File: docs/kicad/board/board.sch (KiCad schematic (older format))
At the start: 17 parts, among them J1 VIN, J10 WHEEL_4, J11 FLAG, J12 LED, J13 COMPASS, J14 SWITCH, J2 LEFT, J3 RIGHT, J4 UNUSED, J5 ARM, J6 LID, J7 WHEEL_1, J8 WHEEL_2, J9 WHEEL_3, SW1 BUTTON_1, SW2 BUTTON_2, U1 ARDUINO_NANO

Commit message: Built version 2 for Daniel
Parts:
- removed J4: UNUSED, cnc3018-PCB:my4pin, symbol Connector_Generic:Conn_01x04
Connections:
- net U_IR: no longer names the net of U1.12 (A0)
- net U_SENS: no longer names the net of U1.15 (D13)
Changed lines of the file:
@@
 Text GLabel 4850 3050 1    50   Input ~ 0
 R_IR
-Text GLabel 5150 3050 1    50   Input ~ 0
-U_IR
 Text GLabel 4550 3050 1    50   Input ~ 0
 L_SENS
 Text GLabel 4950 3050 1    50   Input ~ 0
 R_SENS
-Text GLabel 5450 3050 1    50   Input ~ 0
-U_SENS
 Text GLabel 4650 3850 3    50   Input ~ 0
 WHEEL_1
@@
 	-1   0    0    1
 $EndComp
-$Comp
-L Connector_Generic:Conn_01x04 J4
-U 1 1 63300773
-P 4650 1350
-F 0 "J4" V 4850 1350 50  0000 R CNN
-F 1 "UNUSED" V 4750 1300 50  0000 C CNN
-F 2 "cnc3018-PCB:my4pin" H 4650 1350 50  0001 C CNN
-F 3 "~" H 4650 1350 50  0001 C CNN
-	1    4650 1350
-	0    -1   -1   0
-$EndComp
-$Comp
-L power:GND #PWR06
-U 1 1 63300779
-P 4550 1550
-F 0 "#PWR06" H 4550 1300 50  0001 C CNN
-F 1 "GND" V 4550 1350 50  0000 C CNN
-F 2 "" H 4550 1550 50  0001 C CNN
-F 3 "" H 4550 1550 50  0001 C CNN
-	1    4550 1550
-	1    0    0    -1
-$EndComp
-$Comp
-L power:+5V #PWR07
-U 1 1 6330077F
-P 4650 1550
-F 0 "#PWR07" H 4650 1400 50  0001 C CNN
-F 1 "+5V" V 4650 1750 50  0000 C CNN
-F 2 "" H 4650 1550 50  0001 C CNN
-F 3 "" H 4650 1550 50  0001 C CNN
-	1    4650 1550
-	-1   0    0    1
-$EndComp
 Text GLabel 3700 1550 3    50   Input ~ 0
 L_SENS
-Text GLabel 4850 1550 3    50   Input ~ 0
-U_SENS
 Text GLabel 4300 1550 3    50   Input ~ 0
 R_SENS
 Text GLabel 3600 1550 3    50   Input ~ 0
 L_IR
-Text GLabel 4750 1550 3    50   Input ~ 0
-U_IR
 Text GLabel 4200 1550 3    50   Input ~ 0
 R_IR

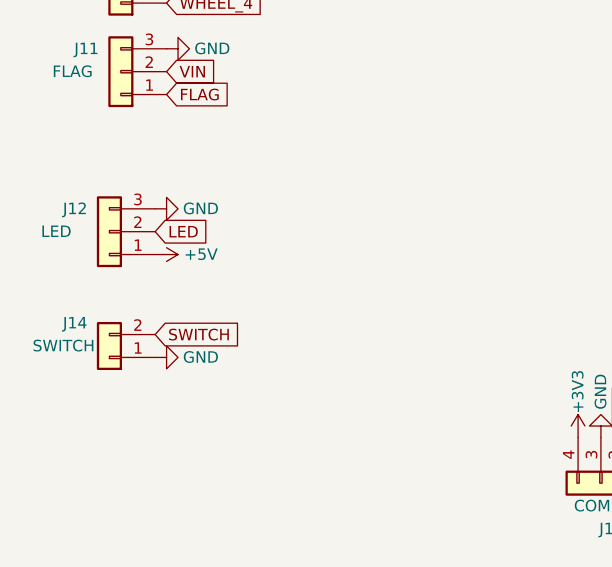
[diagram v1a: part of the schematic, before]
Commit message: created 3D rendering of PCB with my new kicad footprint files
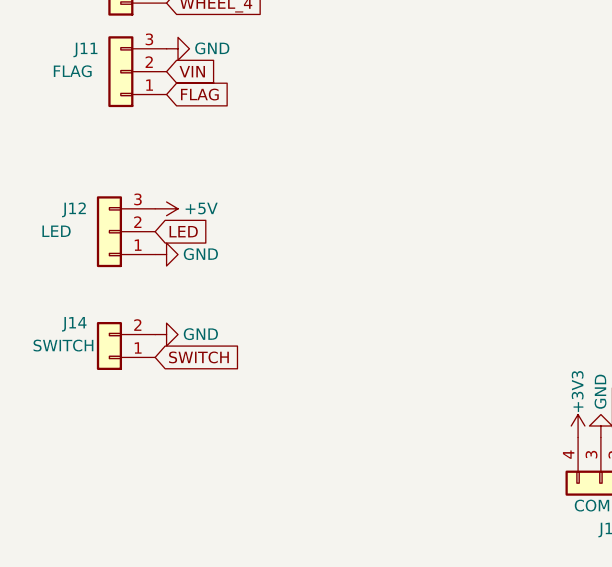
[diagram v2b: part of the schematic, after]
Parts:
- J1, J14: footprint cnc3018-PCB:my2pin -> 0_my_footprints:myJSTx02
- J10, J11, J5, J6, J7, J8, J9: footprint cnc3018-PCB:my3pin -> Connector_PinHeader_2.54mm:PinHeader_1x03_P2.54mm_Vertical
- J12: footprint cnc3018-PCB:my3pin -> 0_my_footprints:myJSTx03
- J13: footprint cnc3018-PCB:my4pin -> 0_my_footprints:myPinSocket_1x04
- J2, J3: footprint cnc3018-PCB:my4pin -> 0_my_footprints:myJSTx04
- SW1, SW2: footprint cnc3018-PCB:right_angle_button -> 0_my_footprints:myButtonAngled
- U1: footprint cnc3018-PCB:ARDUINO_NANO -> 0_my_footprints:myArduinoNano
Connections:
- net +5V: now also J12.3 (Pin_3); no longer J12.1 (Pin_1)
- net GND: now also J12.1 (Pin_1), J14.2 (Pin_2); no longer J12.3 (Pin_3), J14.1 (Pin_1)
- net SWITCH: now also J14.1 (Pin_1); no longer J14.2 (Pin_2)
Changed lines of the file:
@@
 F 0 "U1" H 5528 3496 50  0000 L CNN
 F 1 "ARDUINO_NANO" H 5528 3405 50  0000 L CNN
-F 2 "cnc3018-PCB:ARDUINO_NANO" H 4350 3450 50  0001 C CNN
+F 2 "0_my_footprints:myArduinoNano" H 4350 3450 50  0001 C CNN
 F 3 "" H 4350 3450 50  0001 C CNN
 	1    4700 3450
@@
 F 0 "J1" H 1550 900 50  0000 C CNN
 F 1 "VIN" H 1550 1000 50  0000 C CNN
-F 2 "cnc3018-PCB:my2pin" H 1400 1050 50  0001 C CNN
+F 2 "0_my_footprints:myJSTx02" H 1400 1050 50  0001 C CNN
 F 3 "~" H 1400 1050 50  0001 C CNN
 	1    1400 1050
@@
 F 0 "J5" H 1550 1600 50  0000 C CNN
 F 1 "ARM" H 1650 1700 50  0000 R CNN
-F 2 "cnc3018-PCB:my3pin" H 1400 1700 50  0001 C CNN
+F 2 "Connector_PinHeader_2.54mm:PinHeader_1x03_P2.54mm_Vertical" H 1400 1700 50  0001 C CNN
 F 3 "~" H 1400 1700 50  0001 C CNN
 	1    1400 1700
@@
 F 0 "J6" H 1550 2000 50  0000 C CNN
 F 1 "LID" H 1650 2100 50  0000 R CNN
-F 2 "cnc3018-PCB:my3pin" H 1400 2100 50  0001 C CNN
+F 2 "Connector_PinHeader_2.54mm:PinHeader_1x03_P2.54mm_Vertical" H 1400 2100 50  0001 C CNN
 F 3 "~" H 1400 2100 50  0001 C CNN
 	1    1400 2100
@@
 F 0 "J7" H 1550 2400 50  0000 C CNN
 F 1 "WHEEL_1" H 1850 2500 50  0000 R CNN
-F 2 "cnc3018-PCB:my3pin" H 1400 2500 50  0001 C CNN
+F 2 "Connector_PinHeader_2.54mm:PinHeader_1x03_P2.54mm_Vertical" H 1400 2500 50  0001 C CNN
 F 3 "~" H 1400 2500 50  0001 C CNN
 	1    1400 2500
@@
 F 0 "J8" H 1550 2800 50  0000 C CNN
 F 1 "WHEEL_2" H 1850 2900 50  0000 R CNN
-F 2 "cnc3018-PCB:my3pin" H 1400 2900 50  0001 C CNN
+F 2 "Connector_PinHeader_2.54mm:PinHeader_1x03_P2.54mm_Vertical" H 1400 2900 50  0001 C CNN
 F 3 "~" H 1400 2900 50  0001 C CNN
 	1    1400 2900
@@
 F 0 "J9" H 1550 3200 50  0000 C CNN
 F 1 "WHEEL_3" H 1850 3300 50  0000 R CNN
-F 2 "cnc3018-PCB:my3pin" H 1400 3300 50  0001 C CNN
+F 2 "Connector_PinHeader_2.54mm:PinHeader_1x03_P2.54mm_Vertical" H 1400 3300 50  0001 C CNN
 F 3 "~" H 1400 3300 50  0001 C CNN
 	1    1400 3300
@@
 F 0 "J10" H 1550 3600 50  0000 C CNN
 F 1 "WHEEL_4" H 1850 3700 50  0000 R CNN
-F 2 "cnc3018-PCB:my3pin" H 1400 3700 50  0001 C CNN
+F 2 "Connector_PinHeader_2.54mm:PinHeader_1x03_P2.54mm_Vertical" H 1400 3700 50  0001 C CNN
 F 3 "~" H 1400 3700 50  0001 C CNN
 	1    1400 3700
@@
 F 0 "J11" H 1550 4000 50  0000 C CNN
 F 1 "FLAG" H 1700 4100 50  0000 R CNN
-F 2 "cnc3018-PCB:my3pin" H 1400 4100 50  0001 C CNN
+F 2 "Connector_PinHeader_2.54mm:PinHeader_1x03_P2.54mm_Vertical" H 1400 4100 50  0001 C CNN
 F 3 "~" H 1400 4100 50  0001 C CNN
 	1    1400 4100
@@
 F 0 "J2" V 3700 1350 50  0000 R CNN
 F 1 "LEFT" V 3600 1300 50  0000 C CNN
-F 2 "cnc3018-PCB:my4pin" H 3500 1350 50  0001 C CNN
+F 2 "0_my_footprints:myJSTx04" H 3500 1350 50  0001 C CNN
 F 3 "~" H 3500 1350 50  0001 C CNN
 	1    3500 1350
@@
 F 0 "J3" V 4300 1350 50  0000 R CNN
 F 1 "RIGHT" V 4200 1300 50  0000 C CNN
-F 2 "cnc3018-PCB:my4pin" H 4100 1350 50  0001 C CNN
+F 2 "0_my_footprints:myJSTx04" H 4100 1350 50  0001 C CNN
 F 3 "~" H 4100 1350 50  0001 C CNN
 	1    4100 1350
@@
 F 0 "J12" H 1500 4700 50  0000 C CNN
 F 1 "LED" H 1650 4800 50  0000 R CNN
-F 2 "cnc3018-PCB:my3pin" H 1350 4800 50  0001 C CNN
+F 2 "0_my_footprints:myJSTx03" H 1350 4800 50  0001 C CNN
 F 3 "~" H 1350 4800 50  0001 C CNN
 	1    1350 4800
@@
 L power:GND #PWR022
 U 1 1 63327EFF
+P 1550 4900
+F 0 "#PWR022" H 1550 4650 50  0001 C CNN
+F 1 "GND" V 1550 4700 50  0000 C CNN
+F 2 "" H 1550 4900 50  0001 C CNN
+F 3 "" H 1550 4900 50  0001 C CNN
+	1    1550 4900
+	0    -1   -1   0
+$EndComp
+$Comp
+L power:+5V #PWR023
+U 1 1 6332BC14
 P 1550 4700
-F 0 "#PWR022" H 1550 4450 50  0001 C CNN
-F 1 "GND" V 1550 4500 50  0000 C CNN
+F 0 "#PWR023" H 1550 4550 50  0001 C CNN
+F 1 "+5V" V 1550 4900 50  0000 C CNN
 F 2 "" H 1550 4700 50  0001 C CNN
 F 3 "" H 1550 4700 50  0001 C CNN
 	1    1550 4700
-	0    -1   -1   0
-$EndComp
-$Comp
-L power:+5V #PWR023
-U 1 1 6332BC14
-P 1550 4900
-F 0 "#PWR023" H 1550 4750 50  0001 C CNN
-F 1 "+5V" V 1550 5100 50  0000 C CNN
-F 2 "" H 1550 4900 50  0001 C CNN
-F 3 "" H 1550 4900 50  0001 C CNN
-	1    1550 4900
 	0    1    1    0
 $EndComp
@@
 F 0 "J13" V 3800 5900 50  0000 R CNN
 F 1 "COMPASS" V 3700 5850 50  0000 C CNN
-F 2 "cnc3018-PCB:my4pin" H 3600 5900 50  0001 C CNN
+F 2 "0_my_footprints:myPinSocket_1x04" H 3600 5900 50  0001 C CNN
 F 3 "~" H 3600 5900 50  0001 C CNN
 	1    3600 5900
@@
 F 0 "SW1" H 6850 1935 50  0000 C CNN
 F 1 "BUTTON_1" H 6850 1844 50  0000 C CNN
-F 2 "cnc3018-PCB:right_angle_button" H 6850 1700 50  0001 C CNN
+F 2 "0_my_footprints:myButtonAngled" H 6850 1700 50  0001 C CNN
 F 3 "~" H 6850 1700 50  0001 C CNN
 	1    6850 1700
@@
 F 0 "SW2" H 6850 2385 50  0000 C CNN
 F 1 "BUTTON_2" H 6850 2294 50  0000 C CNN
-F 2 "cnc3018-PCB:right_angle_button" H 6850 2150 50  0001 C CNN
+F 2 "0_my_footprints:myButtonAngled" H 6850 2150 50  0001 C CNN
 F 3 "~" H 6850 2150 50  0001 C CNN
 	1    6850 2150
@@
 BUT_2
 $Comp
+L power:GND #PWR0101
+U 1 1 6338713B
+P 1550 5250
+F 0 "#PWR0101" H 1550 5000 50  0001 C CNN
+F 1 "GND" V 1550 5050 50  0000 C CNN
+F 2 "" H 1550 5250 50  0001 C CNN
+F 3 "" H 1550 5250 50  0001 C CNN
+	1    1550 5250
+	0    -1   -1   0
+$EndComp
+Text GLabel 1550 5350 2    50   Input ~ 0
+SWITCH
+Text GLabel 5150 3850 3    50   Input ~ 0
+SWITCH
+Text Notes 7800 7000 0    50   ~ 0
+Note: this is the correct schematic for the "fixed" V1 board.\nIf I make another boartd, I should rework pin assignements\nA6 and A7 CANNOT be outputs (for IR Leds) ...
+$Comp
 L Connector_Generic:Conn_01x02 J14
 U 1 1 63387135
@@
 F 0 "J14" H 1500 5200 50  0000 C CNN
 F 1 "SWITCH" H 1550 5300 50  0000 C CNN
-F 2 "cnc3018-PCB:my2pin" H 1350 5350 50  0001 C CNN
+F 2 "0_my_footprints:myJSTx02" H 1350 5350 50  0001 C CNN
 F 3 "~" H 1350 5350 50  0001 C CNN
 	1    1350 5350
 	-1   0    0    1
 $EndComp
-$Comp
-L power:GND #PWR0101
-U 1 1 6338713B
-P 1550 5350
-F 0 "#PWR0101" H 1550 5100 50  0001 C CNN
-F 1 "GND" V 1550 5150 50  0000 C CNN
-F 2 "" H 1550 5350 50  0001 C CNN
-F 3 "" H 1550 5350 50  0001 C CNN
-	1    1550 5350
-	0    -1   -1   0
-$EndComp
-Text GLabel 1550 5250 2    50   Input ~ 0
-SWITCH
-Text GLabel 5150 3850 3    50   Input ~ 0
-SWITCH
-Text Notes 7800 7000 0    50   ~ 0
-Note: this is the correct schematic for the "fixed" V1 board.\nIf I make another boartd, I should rework pin assignements\nA6 and A7 CANNOT be outputs (for IR Leds) ...
 $EndSCHEMATC

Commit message: commit new board schematic using my new symbols and 3D footprints
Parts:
- J10, J11, J5, J6, J7, J8, J9: footprint Connector_PinHeader_2.54mm:PinHeader_1x03_P2.54mm_Vertical -> 0_my_footprints:myPinHeader_1x03
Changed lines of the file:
@@
 F 0 "J5" H 1550 1600 50  0000 C CNN
 F 1 "ARM" H 1650 1700 50  0000 R CNN
-F 2 "Connector_PinHeader_2.54mm:PinHeader_1x03_P2.54mm_Vertical" H 1400 1700 50  0001 C CNN
+F 2 "0_my_footprints:myPinHeader_1x03" H 1400 1700 50  0001 C CNN
 F 3 "~" H 1400 1700 50  0001 C CNN
 	1    1400 1700
@@
 F 0 "J6" H 1550 2000 50  0000 C CNN
 F 1 "LID" H 1650 2100 50  0000 R CNN
-F 2 "Connector_PinHeader_2.54mm:PinHeader_1x03_P2.54mm_Vertical" H 1400 2100 50  0001 C CNN
+F 2 "0_my_footprints:myPinHeader_1x03" H 1400 2100 50  0001 C CNN
 F 3 "~" H 1400 2100 50  0001 C CNN
 	1    1400 2100
@@
 F 0 "J7" H 1550 2400 50  0000 C CNN
 F 1 "WHEEL_1" H 1850 2500 50  0000 R CNN
-F 2 "Connector_PinHeader_2.54mm:PinHeader_1x03_P2.54mm_Vertical" H 1400 2500 50  0001 C CNN
+F 2 "0_my_footprints:myPinHeader_1x03" H 1400 2500 50  0001 C CNN
 F 3 "~" H 1400 2500 50  0001 C CNN
 	1    1400 2500
@@
 F 0 "J8" H 1550 2800 50  0000 C CNN
 F 1 "WHEEL_2" H 1850 2900 50  0000 R CNN
-F 2 "Connector_PinHeader_2.54mm:PinHeader_1x03_P2.54mm_Vertical" H 1400 2900 50  0001 C CNN
+F 2 "0_my_footprints:myPinHeader_1x03" H 1400 2900 50  0001 C CNN
 F 3 "~" H 1400 2900 50  0001 C CNN
 	1    1400 2900
@@
 F 0 "J9" H 1550 3200 50  0000 C CNN
 F 1 "WHEEL_3" H 1850 3300 50  0000 R CNN
-F 2 "Connector_PinHeader_2.54mm:PinHeader_1x03_P2.54mm_Vertical" H 1400 3300 50  0001 C CNN
+F 2 "0_my_footprints:myPinHeader_1x03" H 1400 3300 50  0001 C CNN
 F 3 "~" H 1400 3300 50  0001 C CNN
 	1    1400 3300
@@
 F 0 "J10" H 1550 3600 50  0000 C CNN
 F 1 "WHEEL_4" H 1850 3700 50  0000 R CNN
-F 2 "Connector_PinHeader_2.54mm:PinHeader_1x03_P2.54mm_Vertical" H 1400 3700 50  0001 C CNN
+F 2 "0_my_footprints:myPinHeader_1x03" H 1400 3700 50  0001 C CNN
 F 3 "~" H 1400 3700 50  0001 C CNN
 	1    1400 3700
@@
 F 0 "J11" H 1550 4000 50  0000 C CNN
 F 1 "FLAG" H 1700 4100 50  0000 R CNN
-F 2 "Connector_PinHeader_2.54mm:PinHeader_1x03_P2.54mm_Vertical" H 1400 4100 50  0001 C CNN
+F 2 "0_my_footprints:myPinHeader_1x03" H 1400 4100 50  0001 C CNN
 F 3 "~" H 1400 4100 50  0001 C CNN
 	1    1400 4100

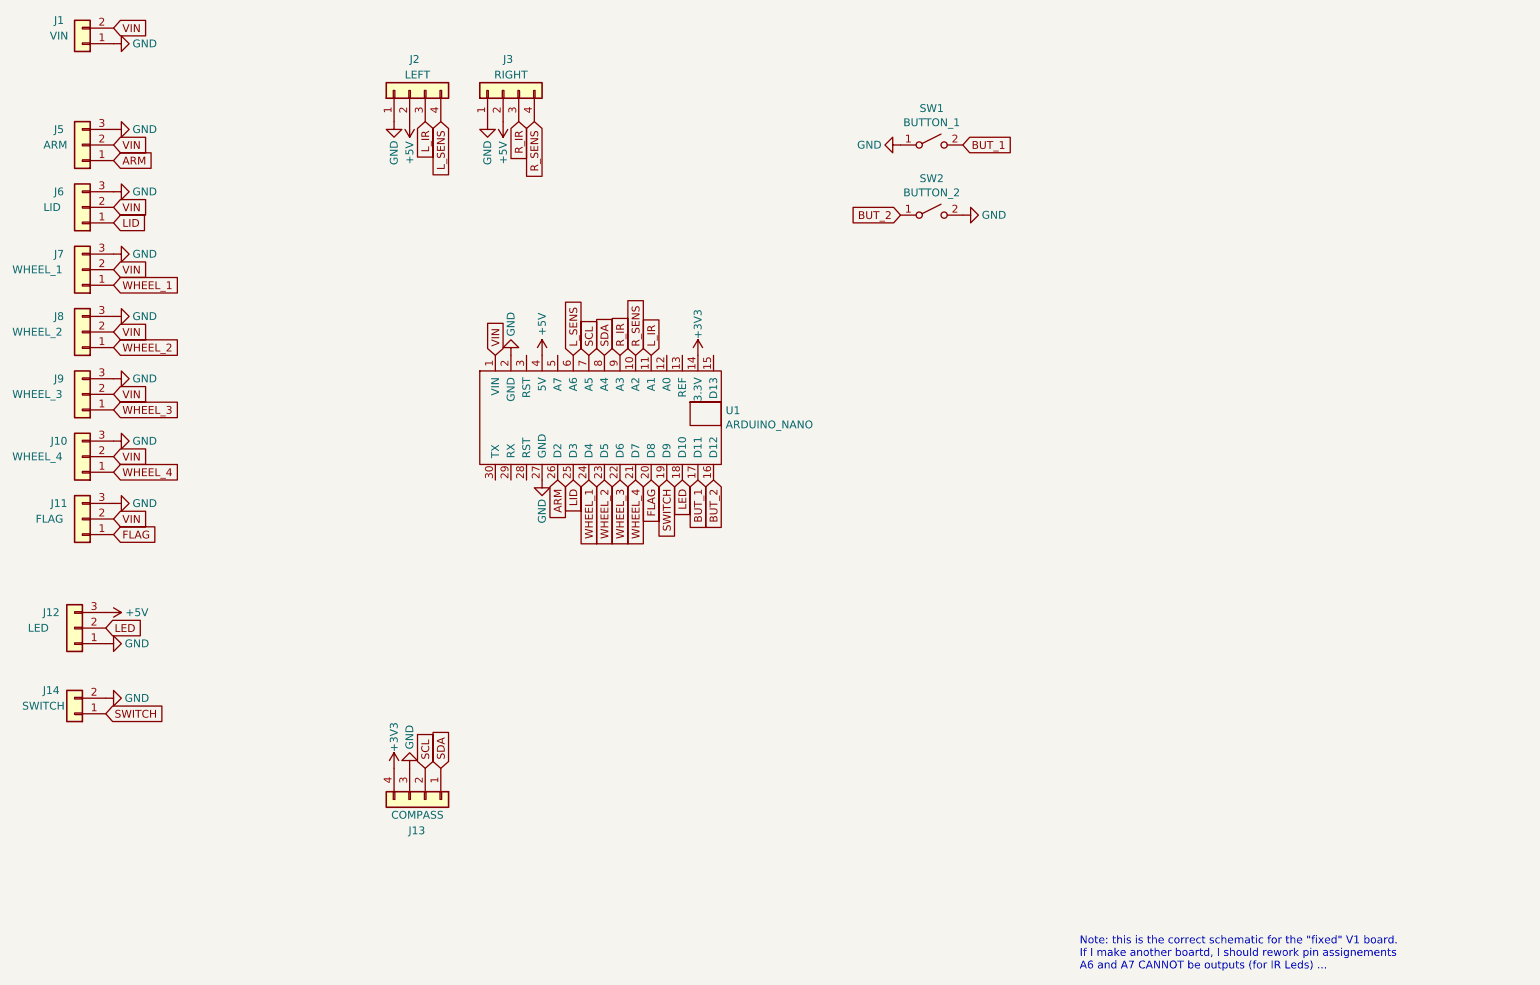
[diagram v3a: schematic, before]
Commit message: SIMPLIFY: got rid of buttons and compass, smaller PCB, all new outputs
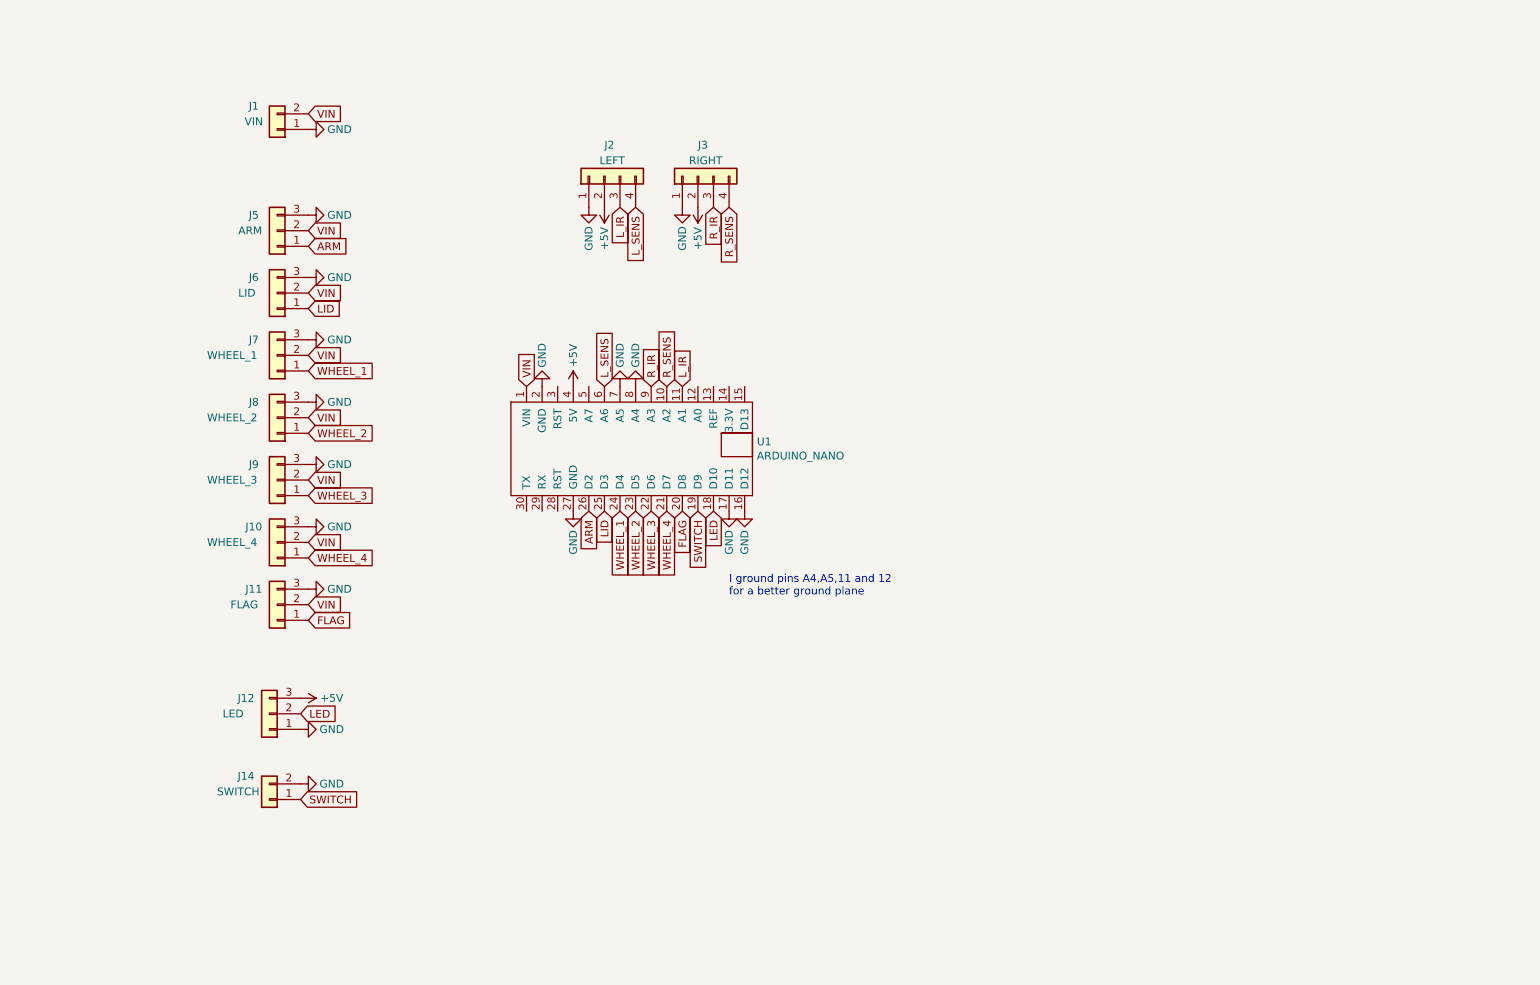
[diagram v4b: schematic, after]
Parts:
- removed J13: COMPASS, 0_my_footprints:myPinSocket_1x04, symbol Connector_Generic:Conn_01x04
- removed SW1: BUTTON_1, 0_my_footprints:myButtonAngled, symbol Switch:SW_SPST
- removed SW2: BUTTON_2, 0_my_footprints:myButtonAngled, symbol Switch:SW_SPST
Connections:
- net BUT_1 is gone; now on net GND: U1.17 (D11)
- net BUT_2 is gone; now on net GND: U1.16 (D12)
- net SCL is gone; now on net GND: U1.7 (A5)
- net SDA is gone; now on net GND: U1.8 (A4)
- net +3V3: no longer names the net of U1.14 (3.3V)
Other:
- note added: "I ground pins A4,A5,11 and 12\nfor a better ground plane"
- note removed: "Note: this is the correct schematic for the "fixed" V1 board.\nIf I make another boartd, I should rework pin assignements\nA6 and A7 CANNOT be outputs (for IR Leds) ..."
- moved on the sheet: J1, J10, J11, J12, J14, J2, J3, J5, J6, J7, J8, J9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
